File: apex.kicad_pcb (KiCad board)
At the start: 4 copper layers, 65.4 x 30.5 mm, 14 parts, among them J1 USB_C_Receptacle_USB2.0_16P, U1 AP7363-33D-13

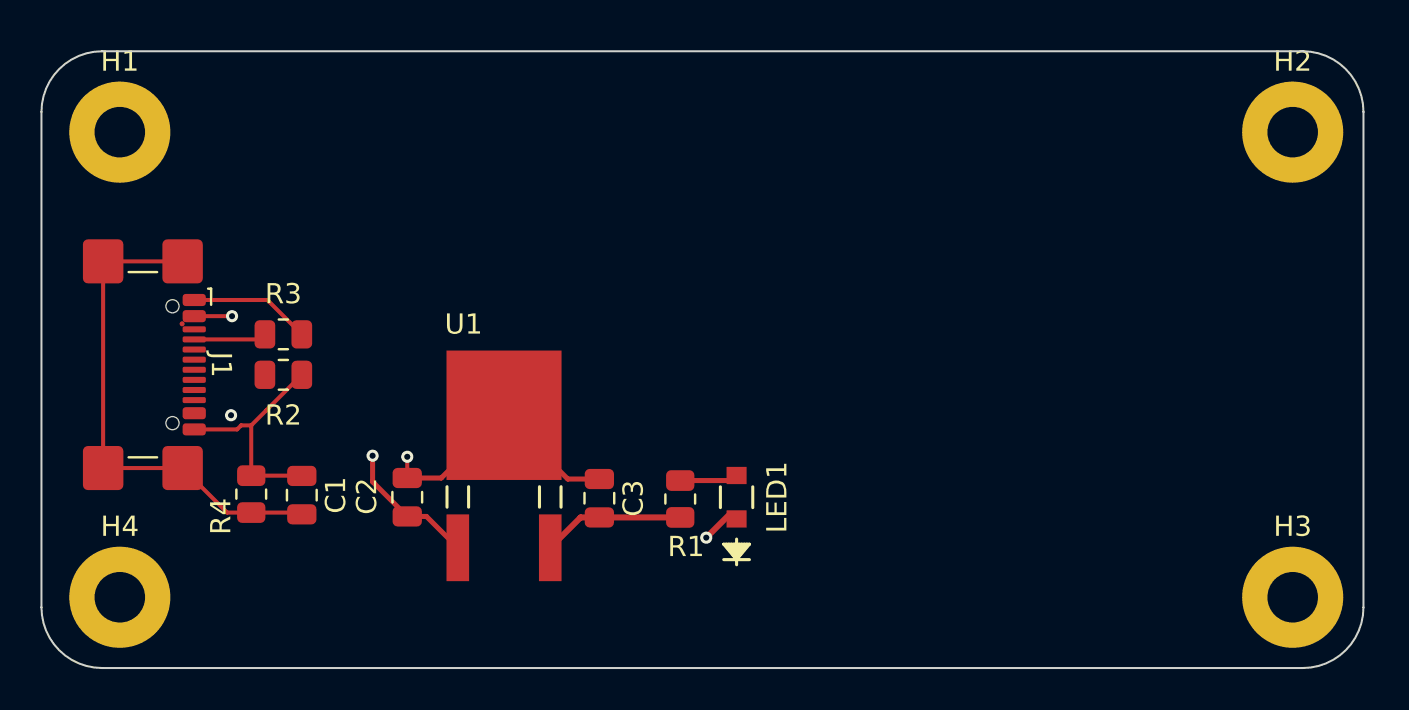
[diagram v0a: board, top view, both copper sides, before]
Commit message: finished ERC, matched footprints, populated 3D models
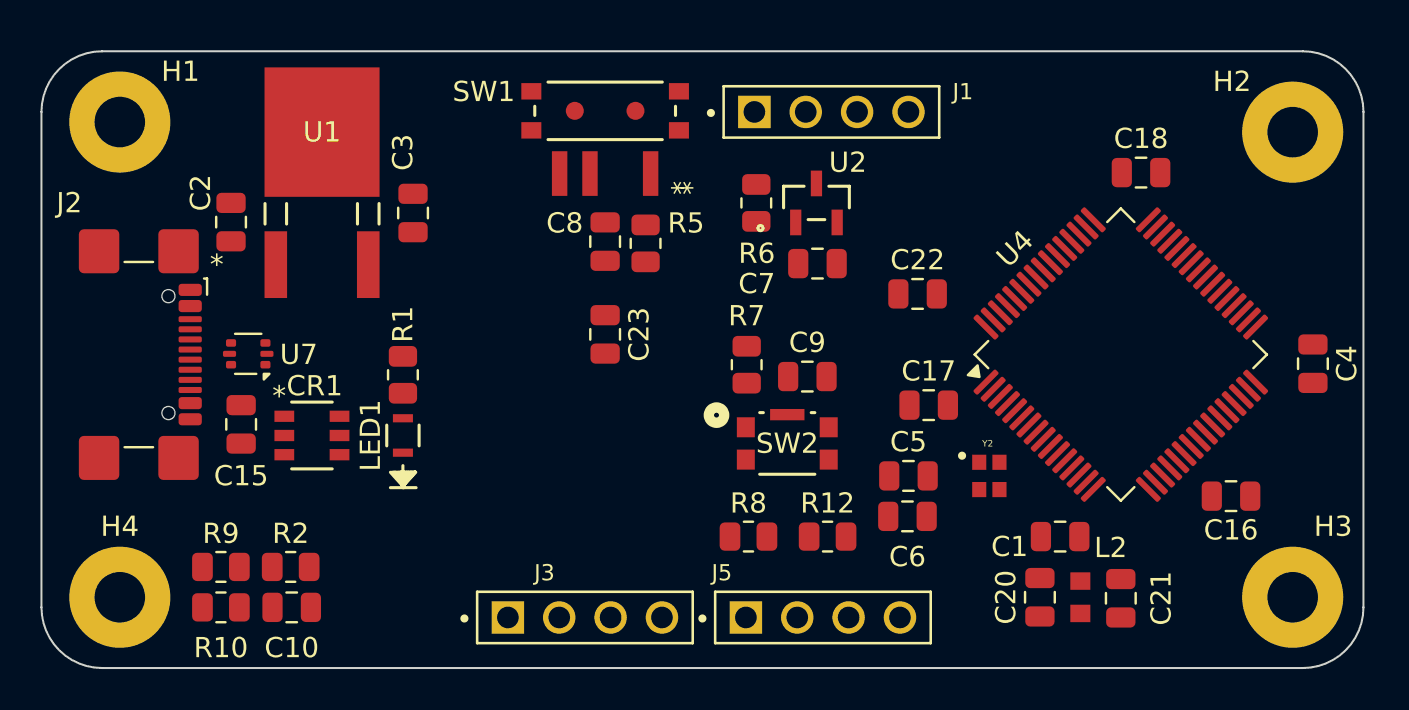
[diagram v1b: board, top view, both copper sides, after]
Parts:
- removed R3: 5.1k, Resistor_SMD:R_0805_2012Metric
- removed R4: 330, Resistor_SMD:R_0805_2012Metric
- added C10: 0.1 uF, Capacitor_SMD:C_0805_2012Metric, F.Cu at (29.0, 58.5)
- added C15: 100 nF, Capacitor_SMD:C_0805_2012Metric, F.Cu at (26.5, 49.5)
- added C16: 100 nF, Capacitor_SMD:C_0805_2012Metric, F.Cu at (75.5, 53.0)
- added C17: 100 nF, Capacitor_SMD:C_0805_2012Metric, F.Cu at (60.5, 48.5)
- added C18: 100 nF, Capacitor_SMD:C_0805_2012Metric, F.Cu at (71.0, 37.0)
- added C20: 1 uF, Capacitor_SMD:C_0805_2012Metric, F.Cu at (66.0, 58.0)
- added C21: 1 uF, Capacitor_SMD:C_0805_2012Metric, F.Cu at (70.0, 58.0)
- added C22: 100 nF, Capacitor_SMD:C_0805_2012Metric, F.Cu at (60.0, 43.0)
- added C23: 10 uF, Capacitor_SMD:C_0805_2012Metric, F.Cu at (44.5, 45.0)
- added C4: 100 nF, Capacitor_SMD:C_0805_2012Metric, F.Cu at (79.5, 46.5)
- added C5: 8 pF, Capacitor_SMD:C_0805_2012Metric, F.Cu at (59.5, 52.0)
- added C6: 8 pF, Capacitor_SMD:C_0805_2012Metric, F.Cu at (59.5, 54.0)
- added C7: 100 nF, Capacitor_SMD:C_0805_2012Metric, F.Cu at (55.0, 41.5)
- added C8: 100 nF, Capacitor_SMD:C_0805_2012Metric, F.Cu at (44.5, 40.4)
- added C9: 47 nF, Capacitor_SMD:C_0805_2012Metric, F.Cu at (54.5, 47.1)
- added CR1: ESDA14V2SC6, ESDA14V2SC6:SOT23-6_1P75X3P05X0P95_STM, F.Cu at (30.0, 50.0)
- added J2: USB_C_Receptacle_USB2.0_16P, Connector_USB:USB_C_Receptacle_GCT_USB4110, F.Cu at (20.3, 46.0)
- added J3: Conn_01x04_Pin, PPTC041LFBN_RC:SULLINS_PPTC041LFBN-RC, F.Cu at (43.5, 59.0)
- added J5: Conn_01x04_Pin, PPTC041LFBN_RC:SULLINS_PPTC041LFBN-RC, F.Cu at (55.3, 59.0)
- added L2: MH1608-121Y, MH1608:IND_BOURNS_MH1608, F.Cu at (68.0, 58.0)
- added R10: 5.1k, Resistor_SMD:R_0805_2012Metric, F.Cu at (25.5, 58.5)
- added R12: 1 K, Resistor_SMD:R_0805_2012Metric, F.Cu at (55.5, 55.0)
- added R5: 10K, Resistor_SMD:R_0805_2012Metric, F.Cu at (46.5, 40.5)
- added R6: 100K, Resistor_SMD:R_0805_2012Metric, F.Cu at (52.0, 38.5)
- added R7: 100K, Resistor_SMD:R_0805_2012Metric, F.Cu at (51.5, 46.5)
- added R8: 1 K, Resistor_SMD:R_0805_2012Metric, F.Cu at (51.6, 55.0)
- added R9: 5.1k, Resistor_SMD:R_0805_2012Metric, F.Cu at (25.5, 56.5)
- added SW1: PCM12SMTR, PCM12SMTR:PCM12SMTR_CNK, F.Cu at (44.5, 33.9)
- added SW2: KMR223G LFG, KMR223_LFG:KMR2_G_CNK, F.Cu at (53.5, 50.4)
- added U2: APX803L20-29SA-7, APX803L20-29-SA-7:SOT23_SA_DIO, F.Cu at (55.0, 38.5)
- added U4: STM32F070RBTx, Package_QFP:LQFP-64_10x10mm_P0.5mm, F.Cu at (70.0, 46.0)
- added U7: USBLC6-2P6, Package_TO_SOT_SMD:SOT-666, F.Cu at (26.9, 46.0)
- added Y2: XRCGB32M000F2P01R0, XRCGB32M000F2P01R0:OSC_XRCGB32M000F2P01R0, F.Cu at (63.5, 52.0)
- C1: value 0.1 uF -> 10 nF
- J1: value USB_C_Receptacle_USB2.0_16P -> Conn_01x04_Pin; footprint Connector_USB:USB_C_Receptacle_GCT_USB4110 -> PPTC041LFBN_RC:SULLINS_PPTC041LFBN-RC
- LED1: footprint LEDBS75000_WRE:LED_BS75000_WRE -> 150080BS75000:LED_BS75000_WRE
- R2: value 5.1k -> 330
- moved C1 37.6 mm to (67.0, 55.0), turned to 0 degrees
- moved J1 37.3 mm to (55.7, 34.0), turned to 0 degrees
- moved C3 16.8 mm to (35.0, 39.0)
- moved LED1 16.8 mm to (34.5, 50.0)
- moved U1 16.6 mm to (30.5, 35.0)
- moved C2 16.2 mm to (26.0, 39.4)
- moved R1 15.0 mm to (34.5, 47.0), turned to 90 degrees
- moved R2 9.51 mm to (28.9, 56.5)
- moved H1 0.50 mm to (20.5, 34.5)
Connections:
- C1 pad 2: GNDPWR -> +3.3 VA
- C3 pad 2: +3V3 -> +3.3 V
- R1 pad 2: +3V3 -> +3.3 V
- R2 pad 1: Net-(J1-CC2) -> GND
- R2 pad 2: GND -> GNDPWR
- U1 pad 3: +3V3 -> +3.3 V
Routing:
- net GND: track 49.0 -> 0.00 mm, vias 2 -> 0
- net GNDPWR: track 25.0 -> 0.00 mm
- net VBUS: track 22.7 -> 0.00 mm, vias 3 -> 0
- net +3V3: track 7.05 -> 0.00 mm
- net Net-(J1-CC1): track 3.60 -> 0.00 mm
- net Net-(LED1-Pad2): track 2.80 -> 0.00 mm
